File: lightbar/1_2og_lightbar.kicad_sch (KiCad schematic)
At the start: 35 parts, among them J1 Conn_01x03

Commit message: spacing updates, silkscreens and etc
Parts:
- J1: footprint Connector_Molex:Molex_Pico-EZmate_78171-0003_1x03-1MP_P1.20mm_Vertical -> Connector_PinHeader_2.54mm:PinHeader_1x03_P2.54mm_Vertical
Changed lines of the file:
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@@
       (effects (font (size 1.27 1.27)))
     )
-    (property "Footprint" "Connector_Molex:Molex_Pico-EZmate_78171-0003_1x03-1MP_P1.20mm_Vertical" (at 159.893 38.735 0)
+    (property "Footprint" "Connector_PinHeader_2.54mm:PinHeader_1x03_P2.54mm_Vertical" (at 159.893 38.735 0)
       (effects (font (size 1.27 1.27)) hide)
     )

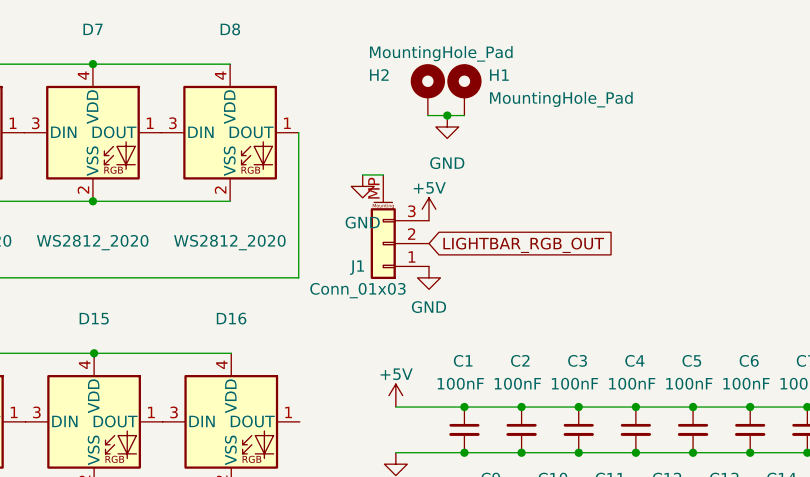
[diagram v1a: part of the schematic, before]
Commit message: update gerbers, change mounting hole dimensions
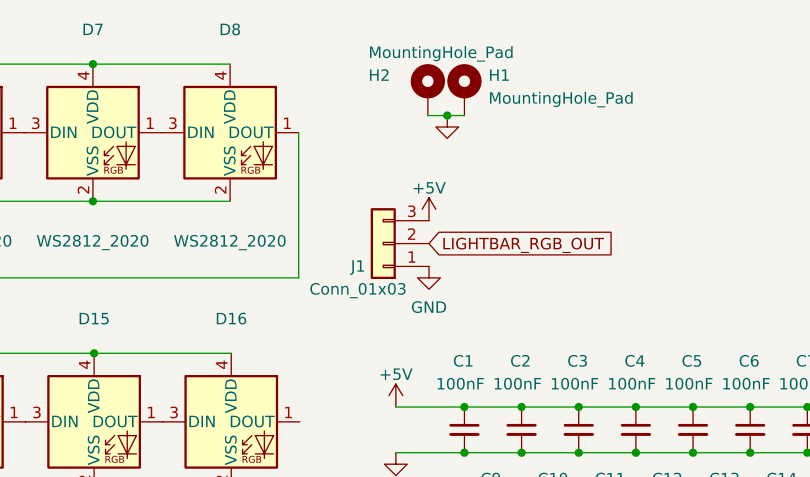
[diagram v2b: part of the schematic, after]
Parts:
- H1, H2: footprint MountingHole:MountingHole_3.2mm_M3_DIN965_Pad_TopBottom -> MountingHole:MountingHole_3mm_Pad
- J1: symbol Connector_Generic_MountingPin:Conn_01x03_MountingPin -> Connector_Generic:Conn_01x03
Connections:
- net GND: no longer J1.MP (MountPin)
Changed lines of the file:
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@@
-    (stroke (width 0) (type default))
-  )
-  (wire (pts (xy 157.607 31.115) (xy 159.893 31.115))
     (stroke (width 0) (type default))
   )
@@
     )
   )
-  (symbol (lib_name "GND_1") (lib_id "power:GND") (at 157.607 31.115 0) (unit 1)
-    (in_bom yes) (on_board yes) (dnp no) (fields_autoplaced)
-    (property "Reference" "#PWR05" (at 157.607 37.465 0)
-      (effects (font (size 1.27 1.27)) hide)
-    )
-    (property "Value" "GND" (at 157.607 36.449 0)
-      (effects (font (size 1.27 1.27)))
-    )
-    (property "Footprint" "" (at 157.607 31.115 0)
-      (effects (font (size 1.27 1.27)) hide)
-    )
-    (property "Datasheet" "" (at 157.607 31.115 0)
-      (effects (font (size 1.27 1.27)) hide)
-    )
-    (pin "1")
-    (instances
-      (project "1_2og_lightbar"
-        (path "/b7d27113-f6cf-475e-bba4-2eec7f4a6a32"
-          (reference "#PWR05") (unit 1)
-        )
-      )
-    )
-  )
   (symbol (lib_id "Device:C_Small") (at 168.91 59.436 0) (unit 1)
     (in_bom yes) (on_board yes) (dnp no)
@@
     )
     (property "Value" "GND" (at 167.005 29.845 0)
-      (effects (font (size 1.27 1.27)))
+      (effects (font (size 1.27 1.27)) hide)
     )
     (property "Footprint" "" (at 167.005 24.511 0)
@@
       (effects (font (size 1.27 1.27)) (justify left))
     )
-    (property "Footprint" "MountingHole:MountingHole_3.2mm_M3_DIN965_Pad_TopBottom" (at 168.91 21.971 0)
+    (property "Footprint" "MountingHole:MountingHole_3mm_Pad" (at 168.91 21.971 0)
       (effects (font (size 1.27 1.27)) hide)
     )
@@
     )
   )
-  (symbol (lib_id "Connector_Generic_MountingPin:Conn_01x03_MountingPin") (at 159.893 38.735 180) (unit 1)
+  (symbol (lib_id "Connector_Generic:Conn_01x03") (at 159.893 38.735 180) (unit 1)
     (in_bom yes) (on_board yes) (dnp no)
     (property "Reference" "J1" (at 157.099 41.275 0)
@@
     (pin "2")
     (pin "3")
-    (pin "MP")
     (instances
       (project "1_2og_lightbar"
@@
       (effects (font (size 1.27 1.27)) (justify left))
     )
-    (property "Footprint" "MountingHole:MountingHole_3.2mm_M3_DIN965_Pad_TopBottom" (at 164.846 21.971 0)
-      (effects (font (size 1.27 1.27)) hide)
-    )
+    (property "Footprint" "MountingHole:MountingHole_3mm_Pad" (at 164.846 21.971 0)
+      (effects (font (size 1.27 1.27)) hide)
+    )

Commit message: idk
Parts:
- added J2: Conn_01x03_Shielded, Connector_Molex:Molex_Pico-EZmate_78171-0003_1x03-1MP_P1.20mm_Vertical, symbol Connector_Generic_MountingPin:Conn_01x03_MountingPin
- added R1, R2: 500, Resistor_SMD:R_0805_2012Metric, symbol Device:R
- C1, C10, C11, C12, C13, C14, C15, C16, C2, C3, C4, C5, C6, C7, C8, C9: LCSC C1525 -> (none)
- D1, D10, D11, D12, D13, D14, D15, D16, D2, D3, D4, D5, D6, D7, D8, D9: value WS2812_2020 -> SK6812_EC15; footprint marbastlib-various:LED_WS2812_2020 -> LED_SMD:LED_SK6812_EC15_1.5x1.5mm; symbol marbastlib-various:WS2812_2020 -> LED:SK6805
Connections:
- net +5V: now also J1.1 (Pin_1), J2.1 (Pin_1); no longer J1.3 (Pin_3)
- net GND: now also J1.3 (Pin_3), J2.3 (Pin_3), J2.MP (MountPin); no longer J1.1 (Pin_1)
- net LIGHTBAR_RGB_OUT: now also J2.2 (Pin_2), R1.1; no longer D1.3 (DIN)
- net at D16.1 (DOUT): now also R2.1
- new net: D1.3 (DIN), R1.2
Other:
- moved on the sheet: D1, D10, D11, D12, D13, D14, D15, D16, D2, D3, D4, D5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
